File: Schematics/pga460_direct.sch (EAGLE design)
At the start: 14 parts, among them IC1 PGA460TPWQ1, T1 BSS84

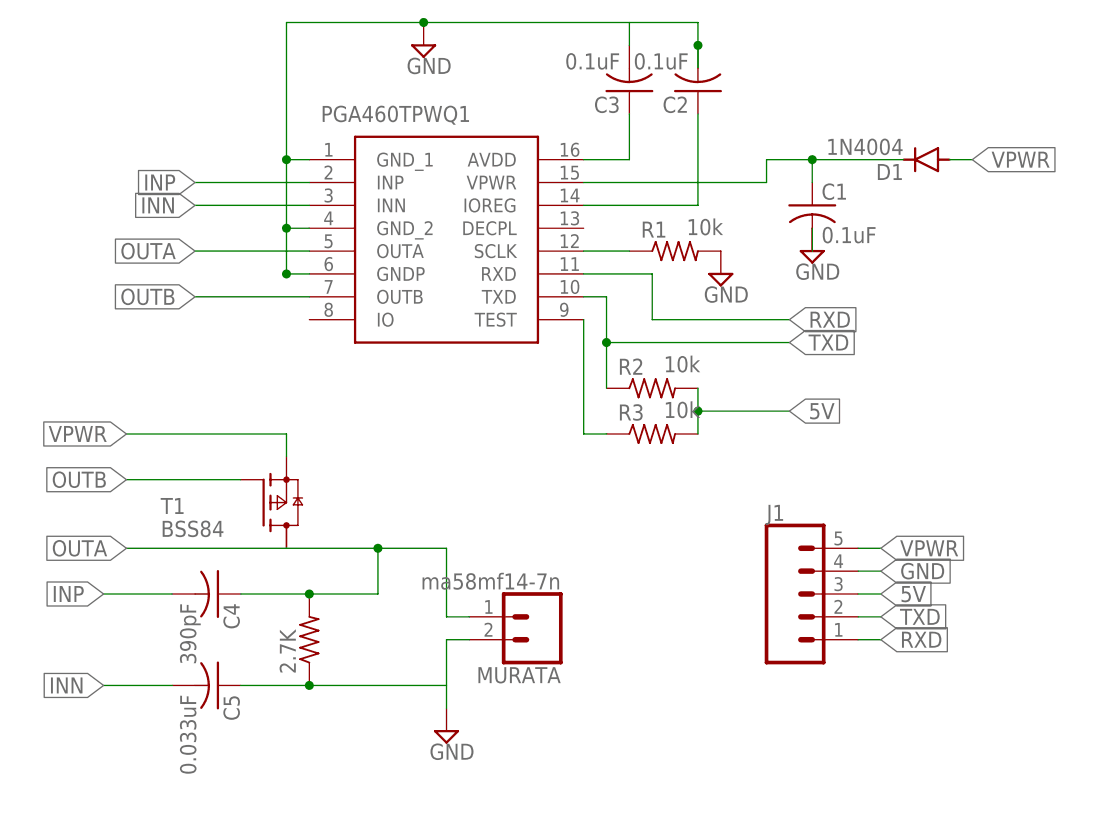
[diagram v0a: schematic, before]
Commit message: Create pcb board for transformer-driven
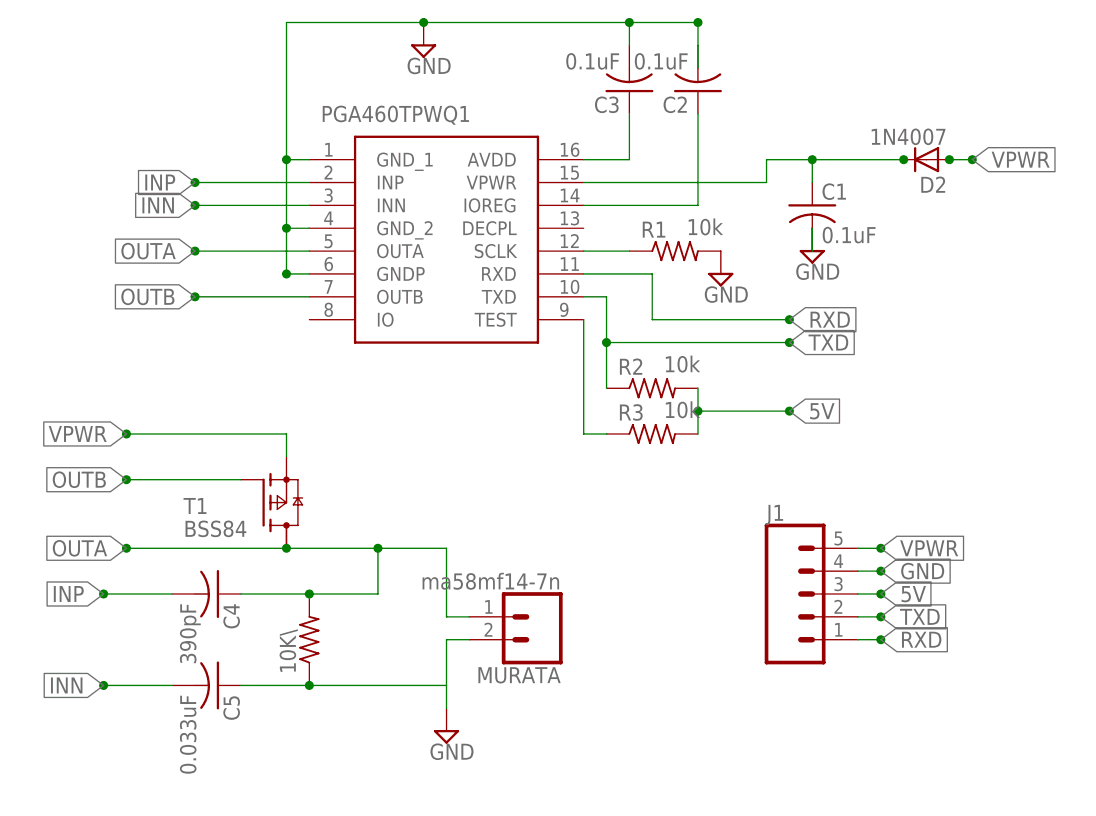
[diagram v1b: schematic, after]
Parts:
- removed D1: 1N4004, diode:1N4004
- added D2: 1N4007, casovac:1N4007
- renumbered 2.7K to 10K\
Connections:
- net N$2: now also D2.C; no longer D1.C
- net VPWR: now also D2.A; no longer D1.A
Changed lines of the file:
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@@
 <parts>
 <part name="IC1" library="PGA460TPWQ1" deviceset="PGA460TPWQ1" device=""/>
-<part name="D1" library="diode" library_urn="urn:adsk.eagle:library:210" deviceset="1N4004" device="" package3d_urn="urn:adsk.eagle:package:43336/1"/>
 <part name="R1" library="rcl" library_urn="urn:adsk.eagle:library:334" deviceset="R-US_" device="R0805" package3d_urn="urn:adsk.eagle:package:23553/2" value="10k"/>
 <part name="R2" library="rcl" library_urn="urn:adsk.eagle:library:334" deviceset="R-US_" device="R0805" package3d_urn="urn:adsk.eagle:package:23553/2" value="10k"/>
@@
 <part name="SUPPLY3" library="supply2" library_urn="urn:adsk.eagle:library:372" deviceset="GND" device=""/>
 <part name="SUPPLY4" library="supply2" library_urn="urn:adsk.eagle:library:372" deviceset="GND" device=""/>
-<part name="2.7K" library="rcl" library_urn="urn:adsk.eagle:library:334" deviceset="R-US_" device="M0805" package3d_urn="urn:adsk.eagle:package:23556/2"/>
+<part name="10K\" library="rcl" library_urn="urn:adsk.eagle:library:334" deviceset="R-US_" device="M0805" package3d_urn="urn:adsk.eagle:package:23556/2"/>
+<part name="D2" library="casovac" deviceset="1N4007" device=""/>
 </parts>
 <sheets>
@@
 <attribute name="VALUE" x="16.51" y="63.5" size="1.778" layer="96" align="center-left"/>
 </instance>
-<instance part="D1" gate="1" x="83.82" y="58.42" smashed="yes" rot="R180">
-<attribute name="NAME" x="81.28" y="57.9374" size="1.778" layer="95" rot="R180"/>
-<attribute name="VALUE" x="81.28" y="60.7314" size="1.778" layer="96" rot="R180"/>
-</instance>
 <instance part="R1" gate="G$1" x="55.88" y="48.26" smashed="yes">
 <attribute name="NAME" x="52.07" y="49.7586" size="1.778" layer="95"/>
@@
 </instance>
 <instance part="T1" gate="G$1" x="12.7" y="20.32" smashed="yes">
-<attribute name="VALUE" x="-1.27" y="16.51" size="1.778" layer="96" font="vector"/>
-<attribute name="NAME" x="-1.27" y="19.05" size="1.778" layer="95" font="vector"/>
+<attribute name="VALUE" x="1.27" y="16.51" size="1.778" layer="96" font="vector"/>
+<attribute name="NAME" x="1.27" y="19.05" size="1.778" layer="95" font="vector"/>
 </instance>
 <instance part="SUPPLY1" gate="GND" x="27.94" y="71.12" smashed="yes">
@@
 <attribute name="VALUE" x="28.575" y="-8.255" size="1.778" layer="96"/>
 </instance>
-<instance part="2.7K" gate="G$1" x="15.24" y="5.08" smashed="yes" rot="R90">
+<instance part="10K\" gate="G$1" x="15.24" y="5.08" smashed="yes" rot="R90">
 <attribute name="NAME" x="13.7414" y="1.27" size="1.778" layer="95" rot="R90"/>
 <attribute name="VALUE" x="18.542" y="1.27" size="1.778" layer="96" rot="R90"/>
+</instance>
+<instance part="D2" gate="G$1" x="83.82" y="58.42" smashed="yes" rot="R180">
+<attribute name="NAME" x="86.106" y="56.515" size="1.778" layer="95" rot="R180"/>
+<attribute name="VALUE" x="86.106" y="61.849" size="1.778" layer="96" rot="R180"/>
 </instance>
 </instances>
@@
 <wire x1="45.72" y1="55.88" x2="66.04" y2="55.88" width="0.1524" layer="91"/>
 <wire x1="66.04" y1="55.88" x2="66.04" y2="58.42" width="0.1524" layer="91"/>
-<pinref part="D1" gate="1" pin="C"/>
 <wire x1="66.04" y1="58.42" x2="71.12" y2="58.42" width="0.1524" layer="91"/>
 <wire x1="81.28" y1="58.42" x2="71.12" y2="58.42" width="0.1524" layer="91"/>
@@
 <wire x1="71.12" y1="58.42" x2="71.12" y2="55.88" width="0.1524" layer="91"/>
 <junction x="71.12" y="58.42"/>
+<pinref part="D2" gate="G$1" pin="C"/>
+<junction x="81.28" y="58.42"/>
 </segment>
 </net>
@@
 <wire x1="15.24" y1="55.88" x2="2.54" y2="55.88" width="0.1524" layer="91"/>
 <label x="2.54" y="55.88" size="1.778" layer="95" rot="R180" xref="yes"/>
+<junction x="2.54" y="55.88"/>
 </segment>
 <segment>
@@
 <wire x1="0" y1="10.16" x2="-7.62" y2="10.16" width="0.1524" layer="91"/>
 <label x="-7.62" y="10.16" size="1.778" layer="95" rot="R180" xref="yes"/>
+<junction x="-7.62" y="10.16"/>
 </segment>
 </net>
@@
 <wire x1="15.24" y1="53.34" x2="2.54" y2="53.34" width="0.1524" layer="91"/>
 <label x="2.54" y="53.34" size="1.778" layer="95" rot="R180" xref="yes"/>
+<junction x="2.54" y="53.34"/>
 </segment>
 <segment>
@@
 <wire x1="0" y1="0" x2="-7.62" y2="0" width="0.1524" layer="91"/>
 <label x="-7.62" y="0" size="1.778" layer="95" rot="R180" xref="yes"/>
+<junction x="-7.62" y="0"/>
 </segment>
 </net>
@@
 <wire x1="15.24" y1="48.26" x2="2.54" y2="48.26" width="0.1524" layer="91"/>
 <label x="2.54" y="48.26" size="1.778" layer="95" rot="R180" xref="yes"/>
-</segment>
-<segment>
-<pinref part="T1" gate="G$1" pin="D"/>
-<wire x1="12.7" y1="15.24" x2="22.86" y2="15.24" width="0.1524" layer="91"/>
-<label x="-5.08" y="15.24" size="1.778" layer="95" rot="R180" xref="yes"/>
+<junction x="2.54" y="48.26"/>
+</segment>
+<segment>
 <wire x1="22.86" y1="15.24" x2="22.86" y2="10.16" width="0.1524" layer="91"/>
 <pinref part="C4" gate="G$1" pin="1"/>
 <wire x1="7.62" y1="10.16" x2="15.24" y2="10.16" width="0.1524" layer="91"/>
-<pinref part="2.7K" gate="G$1" pin="2"/>
+<pinref part="10K\" gate="G$1" pin="2"/>
 <wire x1="15.24" y1="10.16" x2="22.86" y2="10.16" width="0.1524" layer="91"/>
-<wire x1="12.7" y1="15.24" x2="-5.08" y2="15.24" width="0.1524" layer="91"/>
 <junction x="15.24" y="10.16"/>
 <wire x1="22.86" y1="15.24" x2="30.48" y2="15.24" width="0.1524" layer="91"/>
@@
 <pinref part="MURATA" gate="G$1" pin="1"/>
 <wire x1="30.48" y1="7.62" x2="33.02" y2="7.62" width="0.1524" layer="91"/>
+<pinref part="T1" gate="G$1" pin="D"/>
+<wire x1="12.7" y1="15.24" x2="-5.08" y2="15.24" width="0.1524" layer="91"/>
+<junction x="-5.08" y="15.24"/>
+<label x="-5.08" y="15.24" size="1.778" layer="95" rot="R180" xref="yes"/>
+<wire x1="12.7" y1="15.24" x2="22.86" y2="15.24" width="0.1524" layer="91"/>
 <junction x="22.86" y="15.24"/>
+<junction x="12.7" y="15.24"/>
 </segment>
 </net>
@@
 <wire x1="15.24" y1="43.18" x2="2.54" y2="43.18" width="0.1524" layer="91"/>
 <label x="2.54" y="43.18" size="1.778" layer="95" rot="R180" xref="yes"/>
+<junction x="2.54" y="43.18"/>
 </segment>
 <segment>
@@
 <label x="-5.08" y="22.86" size="1.778" layer="95" rot="R180" xref="yes"/>
 <wire x1="7.62" y1="22.86" x2="-5.08" y2="22.86" width="0.1524" layer="91"/>
+<junction x="-5.08" y="22.86"/>
 </segment>
 </net>
@@
 <pinref part="C2" gate="G$1" pin="2"/>
 <wire x1="58.42" y1="71.12" x2="58.42" y2="68.58" width="0.1524" layer="91"/>
-<junction x="58.42" y="71.12"/>
+<junction x="50.8" y="73.66"/>
+<junction x="58.42" y="73.66"/>
 </segment>
 <segment>
@@
 <wire x1="76.2" y1="12.7" x2="78.74" y2="12.7" width="0.1524" layer="91"/>
 <label x="78.74" y="12.7" size="1.778" layer="95" xref="yes"/>
+<junction x="78.74" y="12.7"/>
 </segment>
 <segment>
@@
 <pinref part="C5" gate="G$1" pin="1"/>
 <wire x1="7.62" y1="0" x2="15.24" y2="0" width="0.1524" layer="91"/>
-<pinref part="2.7K" gate="G$1" pin="1"/>
+<pinref part="10K\" gate="G$1" pin="1"/>
 <wire x1="15.24" y1="0" x2="30.48" y2="0" width="0.1524" layer="91"/>
 <junction x="15.24" y="0"/>
@@
 <wire x1="76.2" y1="15.24" x2="78.74" y2="15.24" width="0.1524" layer="91"/>
 <label x="78.74" y="15.24" size="1.778" layer="95" xref="yes"/>
+<junction x="78.74" y="15.24"/>
 </segment>
 <segment>
@@
 <label x="-5.08" y="27.94" size="1.778" layer="95" rot="R180" xref="yes"/>
 <wire x1="12.7" y1="27.94" x2="-5.08" y2="27.94" width="0.1524" layer="91"/>
-</segment>
-<segment>
-<pinref part="D1" gate="1" pin="A"/>
+<junction x="-5.08" y="27.94"/>
+</segment>
+<segment>
 <wire x1="86.36" y1="58.42" x2="88.9" y2="58.42" width="0.1524" layer="91"/>
 <label x="88.9" y="58.42" size="1.778" layer="95" xref="yes"/>
+<pinref part="D2" gate="G$1" pin="A"/>
+<junction x="86.36" y="58.42"/>
+<junction x="88.9" y="58.42"/>
 </segment>
 </net>
@@
 <wire x1="76.2" y1="10.16" x2="78.74" y2="10.16" width="0.1524" layer="91"/>
 <label x="78.74" y="10.16" size="1.778" layer="95" xref="yes"/>
+<junction x="78.74" y="10.16"/>
 </segment>
 <segment>
@@
 <label x="68.58" y="30.48" size="1.778" layer="95" xref="yes"/>
 <junction x="58.42" y="30.48"/>
+<junction x="68.58" y="30.48"/>
 </segment>
 </net>
@@
 <wire x1="76.2" y1="7.62" x2="78.74" y2="7.62" width="0.1524" layer="91"/>
 <label x="78.74" y="7.62" size="1.778" layer="95" xref="yes"/>
+<junction x="78.74" y="7.62"/>
 </segment>
 <segment>
@@
 <label x="68.58" y="38.1" size="1.778" layer="95" xref="yes"/>
 <junction x="48.26" y="38.1"/>
+<junction x="68.58" y="38.1"/>
 </segment>
 </net>
@@
 <wire x1="76.2" y1="5.08" x2="78.74" y2="5.08" width="0.1524" layer="91"/>
 <label x="78.74" y="5.08" size="1.778" layer="95" xref="yes"/>
+<junction x="78.74" y="5.08"/>
 </segment>
 <segment>
@@
 <wire x1="53.34" y1="40.64" x2="68.58" y2="40.64" width="0.1524" layer="91"/>
 <label x="68.58" y="40.64" size="1.778" layer="95" xref="yes"/>
-</segment>
-</net>
+<junction x="68.58" y="40.64"/>
+</segment>
+</net>
